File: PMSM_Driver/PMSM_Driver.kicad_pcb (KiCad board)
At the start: 4 copper layers, 261.6 x 144 mm, 276 parts, among them J1 2606-1101, J10 AFBR-2624Z, J11 AFBR-2624Z, J12 AFBR-2624Z, J13 AFBR-2624Z, J14 AFBR-2624Z, J15 AFBR-2624Z, J16 AFBR-2624Z, J17 2606-1101, J18 2606-1101, J2 AFBR-2624Z, J3 1714971, J4 1714971, J5 1827907, J6 AFBR-2624Z, J7 AFBR-2624Z, J8 AFBR-2624Z, J9 AFBR-2624Z, Q1 BC846, Q10 BC846, Q11 RGCL60TK60, Q12 RGCL60TK60, Q13 RGCL60TK60, Q14 RGCL60TK60, Q15 BC846, Q16 RGCL60TK60, Q17 RGCL60TK60, Q18 RGCL60TK60, Q19 RGCL60TK60, Q2 BC846, Q20 BC846, Q21 BC846, Q22 BC846, Q23 BC846, Q24 BC846, Q3 BC846, Q4 BC846, Q5 RGCL60TK60, Q6 RGCL60TK60, Q7 RGCL60TK60, Q8 RGCL60TK60, Q9 BC846, U1 74LVC1G04, U10 HCPL-3120, U11 HCPL-3120, U12 HCPL-3120, U13 74LVC1G04, U14 74LVC1G04, U15 74LVC1G04, U16 MGJ2D051515SC, U17 MGJ2D051515SC, U18 MGJ2D051515SC, U19 HCPL-3120, U2 MGJ2D051515SC, U20 HCPL-3120, U21 HCPL-3120, U22 74LVC1G04, U23 74LVC1G04, U24 74LVC1G04, U25 MGJ2D051515SC, U26 MGJ2D051515SC, U27 MGJ2D051515SC, U28 HCPL-3120, U29 HCPL-3120, U3 HCPL-3120, U30 HCPL-3120, U31 74LVC1G04, U32 74LVC1G04, U33 MGJ2D051515SC, U34 MGJ2D051515SC, U35 HCPL-3120, U36 HCPL-3120, U37 VS-E5TH3006S2L-M3, U38 VS-E5TH3006S2L-M3, U39 VS-E5TH3006S2L-M3, U4 74LVC1G04, U40 VS-E5TH3006S2L-M3, U41 VS-E5TH3006S2L-M3, U42 VS-E5TH3006S2L-M3, U43 VS-E5TH3006S2L-M3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

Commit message: TBC: filled zone to replace 10A traces, phase-A conpleted
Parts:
- moved J17 4.55 mm to (232.4, 159.0)
- moved H2 4.14 mm to (310.4, 44.5)
- moved H4 3.43 mm to (310.9, 176.0)
- moved J18 2.25 mm to (300.3, 158.6)
- moved J1 1.96 mm to (165.4, 159.0)
- moved J5 1.78 mm to (269.4, 50.9)
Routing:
- net GND: track 287.5 -> 142.1 mm, vias 37 -> 36
- net ib_signal: track 0.00 -> 82.8 mm, vias 1 -> 2
- net ic_signal: track 0.00 -> 64.0 mm
- net ia_out: track 110.4 -> 92.2 mm, vias 23 -> 45
- net /A3_E: track 128.5 -> 121.5 mm, vias 2 -> 41
- net ia_signal: track 134.5 -> 139.7 mm, vias 3 -> 2
- net b_out: track 3.88 -> 1.27 mm, vias 1 -> 0
- net GNDREF: vias 123 -> 96
- net /A1_E: vias 12 -> 21
- net -BATT: vias 112 -> 113
- added copper zone on F.Cu, net /A3_E
- added copper zone on In1.Cu, net /A3_E
- added copper zone on In2.Cu, net /A3_E
- added copper zone on In1.Cu, net a_out
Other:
- board size 261.6 x 144 mm -> 265.6 x 144 mm

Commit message: TBC: modify the overlapped filled zone
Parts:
- C1, C2, C3, C4, C5, C6, C9: moved to B.Cu
- moved C9 99.9 mm to (168.4, 51.6)
- moved C6 84.0 mm to (152.5, 51.6)
- moved C5 68.3 mm to (137.1, 51.8)
- moved C4 52.5 mm to (121.4, 51.9)
- moved C3 36.6 mm to (105.6, 52.0)
- moved C2 20.0 mm to (88.8, 52.1)
- moved U39 7.60 mm to (170.9, 79.0)
- moved U41 7.59 mm to (237.9, 78.1)
- moved C1 5.99 mm to (72.5, 52.1)
- moved U37 2.79 mm to (102.6, 84.1)
- moved C20 0.34 mm to (263.3, 93.6)
- moved C26 0.34 mm to (263.3, 91.3)
- moved C32 0.30 mm to (263.2, 89.0)
- moved C33 0.28 mm to (260.4, 89.0)
- moved C27 0.25 mm to (260.4, 91.2)
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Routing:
- net +5V: track 33.8 -> 257.6 mm
- net /B3_E: track 133.1 -> 80.4 mm, vias 2 -> 0
- net /B1_E: track 130.5 -> 84.6 mm, vias 2 -> 26
- net /A1_E: track 128.4 -> 85.1 mm, vias 21 -> 26
- net /A3_E: track 121.5 -> 82.0 mm, vias 41 -> 31
- net /C1_E: track 127.4 -> 92.8 mm, vias 2 -> 18
- net ia_out: track 92.2 -> 66.6 mm, vias 45 -> 23
- net ib_out: track 103.4 -> 78.9 mm, vias 1 -> 8
- net GND: track 142.1 -> 124.6 mm, vias 36 -> 35
- net c_out: track 14.5 -> 0.07 mm, vias 1 -> 0
- net ia_signal: track 139.7 -> 153.2 mm, vias 2 -> 3
- net ic_signal: track 64.0 -> 77.3 mm
- net b_out: track 1.27 -> 0.00 mm
- net ib_signal: track 82.8 -> 84.0 mm
- net ic_out: track 113.9 -> 113.2 mm
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- added copper zone on In2.Cu, net /A1_E
- added copper zone on F.Cu, net /B1_E
- added copper zone on In2.Cu, net /B1_E
- added copper zone on F.Cu, net /C1_E
- added copper zone on In2.Cu, net /C1_E
- added copper zone on F.Cu, net ib_out
- added copper zone on In1.Cu, net ib_out
- removed copper zone on In1.Cu, net /A1_E
- removed copper zone on In2.Cu, net GNDREF
- removed copper zone on In2.Cu, net ia_out
- removed copper zone on F.Cu, net ic_signal

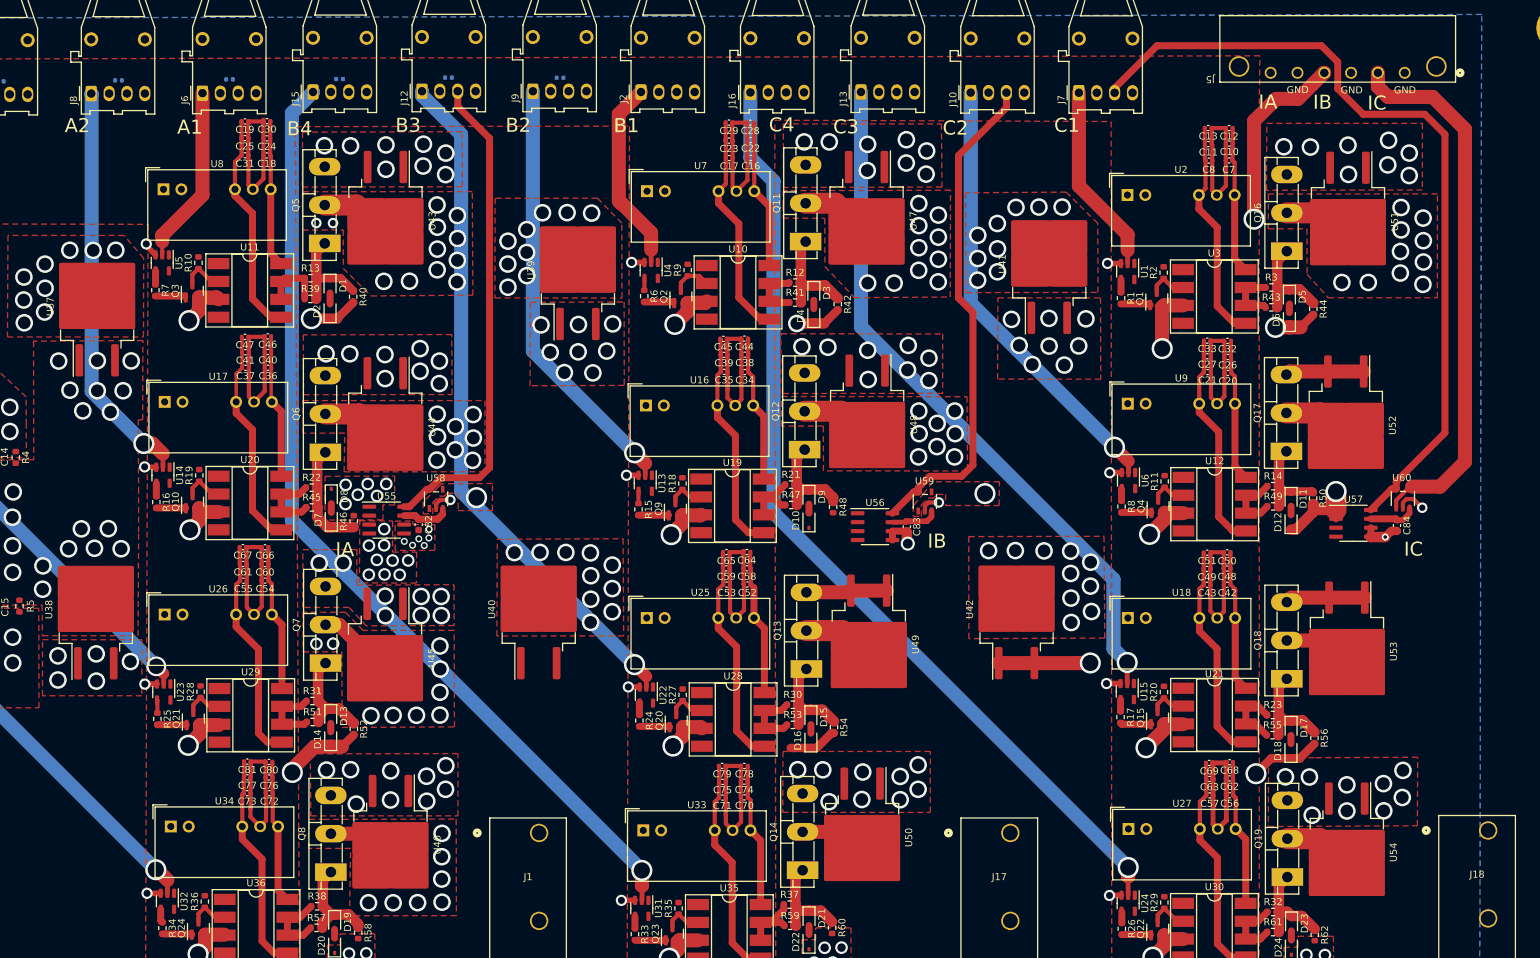
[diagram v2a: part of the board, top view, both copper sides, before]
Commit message: Filled Zone: only Phase C left
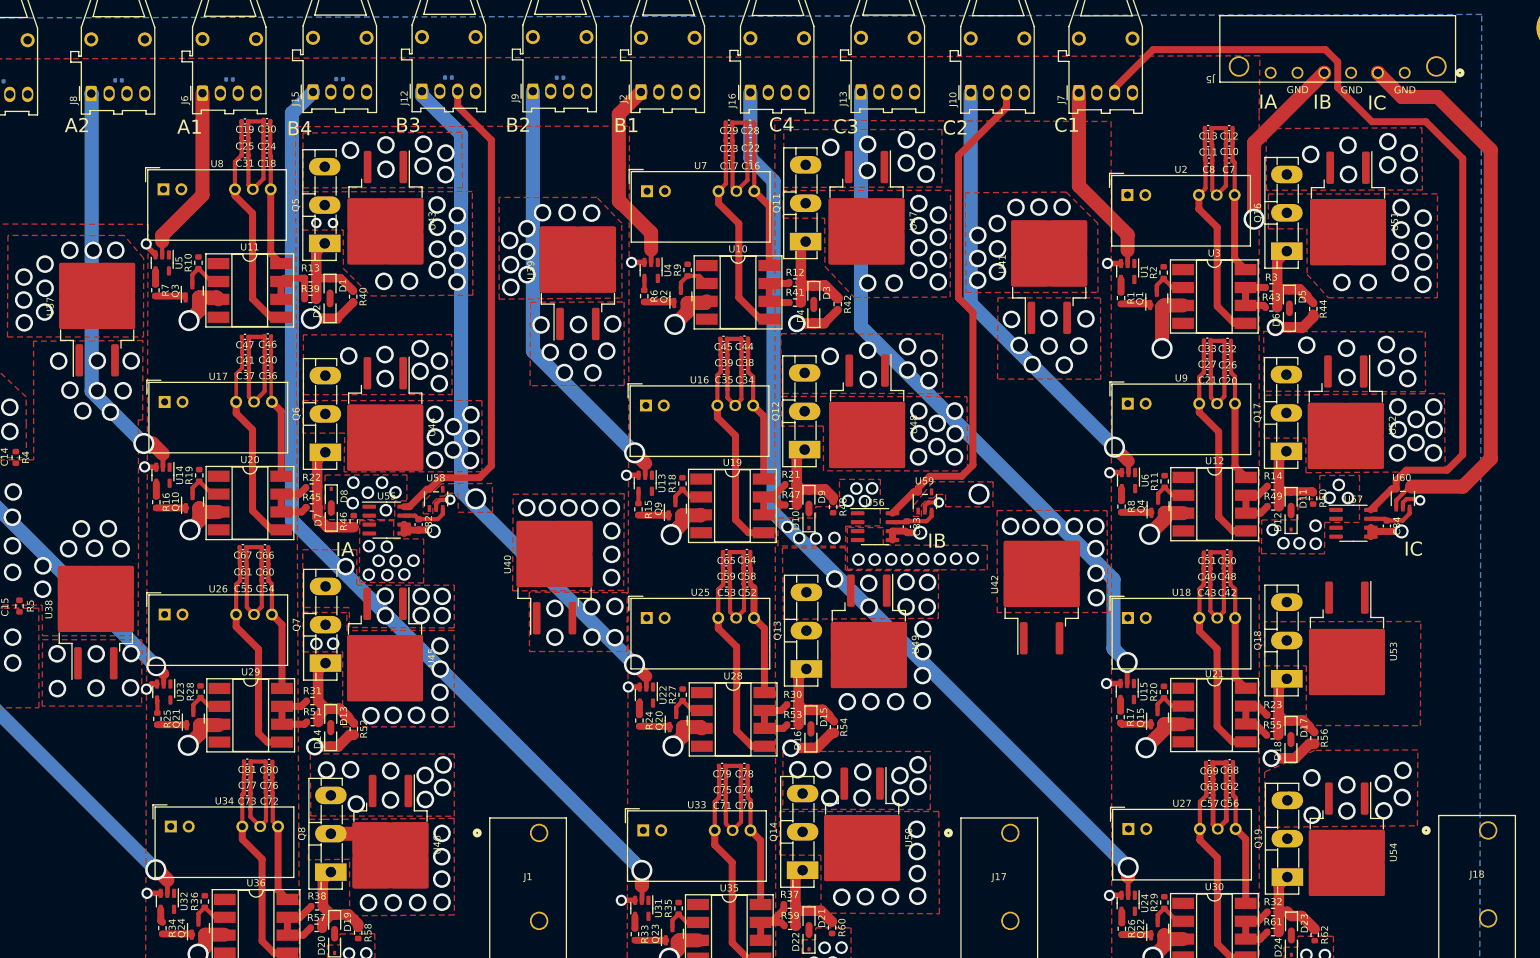
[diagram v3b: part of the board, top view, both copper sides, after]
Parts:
- moved U40 6.77 mm to (167.6, 120.8)
- moved U42 5.02 mm to (236.8, 123.6)
- moved C84 1.43 mm to (285.9, 115.3)
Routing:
- net /C3_E: track 137.7 -> 29.4 mm, vias 2 -> 1
- net ic_out: track 113.2 -> 20.5 mm, vias 1 -> 15
- net /C1_E: track 92.8 -> 28.6 mm, vias 18 -> 25
- net ib_out: track 78.9 -> 23.1 mm, vias 8 -> 22
- net /A1_E: track 85.1 -> 30.3 mm, vias 26 -> 25
- net /B1_E: track 84.6 -> 30.3 mm, vias 26 -> 25
- net /B3_E: track 80.4 -> 28.6 mm, vias 0 -> 31
- net /A3_E: track 82.0 -> 34.4 mm
- net ia_out: track 66.6 -> 23.1 mm, vias 23 -> 22
- net -BATT: track 106.4 -> 66.0 mm, vias 69 -> 68
- net +BATT: track 19.0 -> 0.45 mm
- net ia_signal: track 153.2 -> 162.3 mm, vias 3 -> 2
- net GND: track 124.6 -> 130.3 mm, vias 35 -> 30
- net +5V: track 257.6 -> 262.2 mm
- net ic_signal: track 77.3 -> 81.5 mm
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- added copper zone on F.Cu, net /B3_E
- added copper zone on In1.Cu, net /B3_E
- added copper zone on In2.Cu, net /B3_E
- added copper zone on In1.Cu, net /C3_E
- added copper zone on In2.Cu, net GNDREF
- added copper zone on F.Cu, net b_out
- added copper zone on In1.Cu, net b_out
- added copper zone on F.Cu, net ic_out
- added copper zone on In1.Cu, net ic_out
- removed copper zone on F.Cu, net GND

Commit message: filled zone completed, Fiber-Optic and size of resistors need to be replaced
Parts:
- moved C5 77.8 mm to (61.0, 68.3), turned to -90 degrees
- moved C3 44.9 mm to (63.7, 68.2), turned to -90 degrees
- moved C6 31.3 mm to (121.3, 51.8)
- moved C9 31.2 mm to (137.2, 51.6)
- moved C4 15.8 mm to (105.6, 52.0)
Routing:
- net /C3_E: track 29.4 -> 29.0 mm, vias 1 -> 31
- net ic_out: vias 15 -> 22
- net c_out: vias 0 -> 8
- added copper zone on F.Cu, net /C3_E
- added copper zone on In2.Cu, net /C3_E
- added copper zone on F.Cu, net c_out
- added copper zone on In1.Cu, net c_out

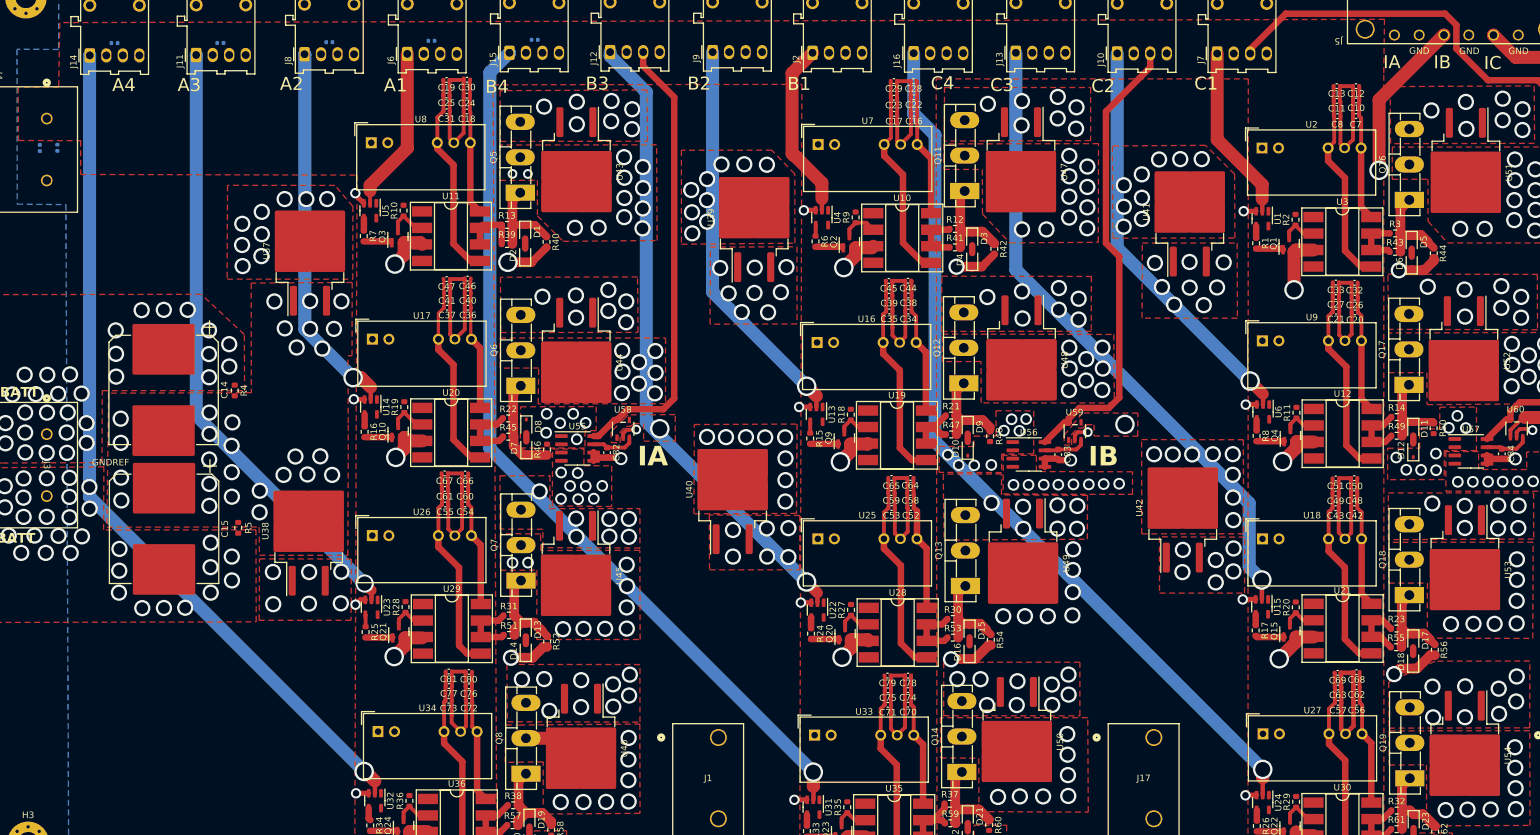
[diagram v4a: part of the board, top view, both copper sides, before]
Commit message: filled zone completed, some SMD components need to be re-selected
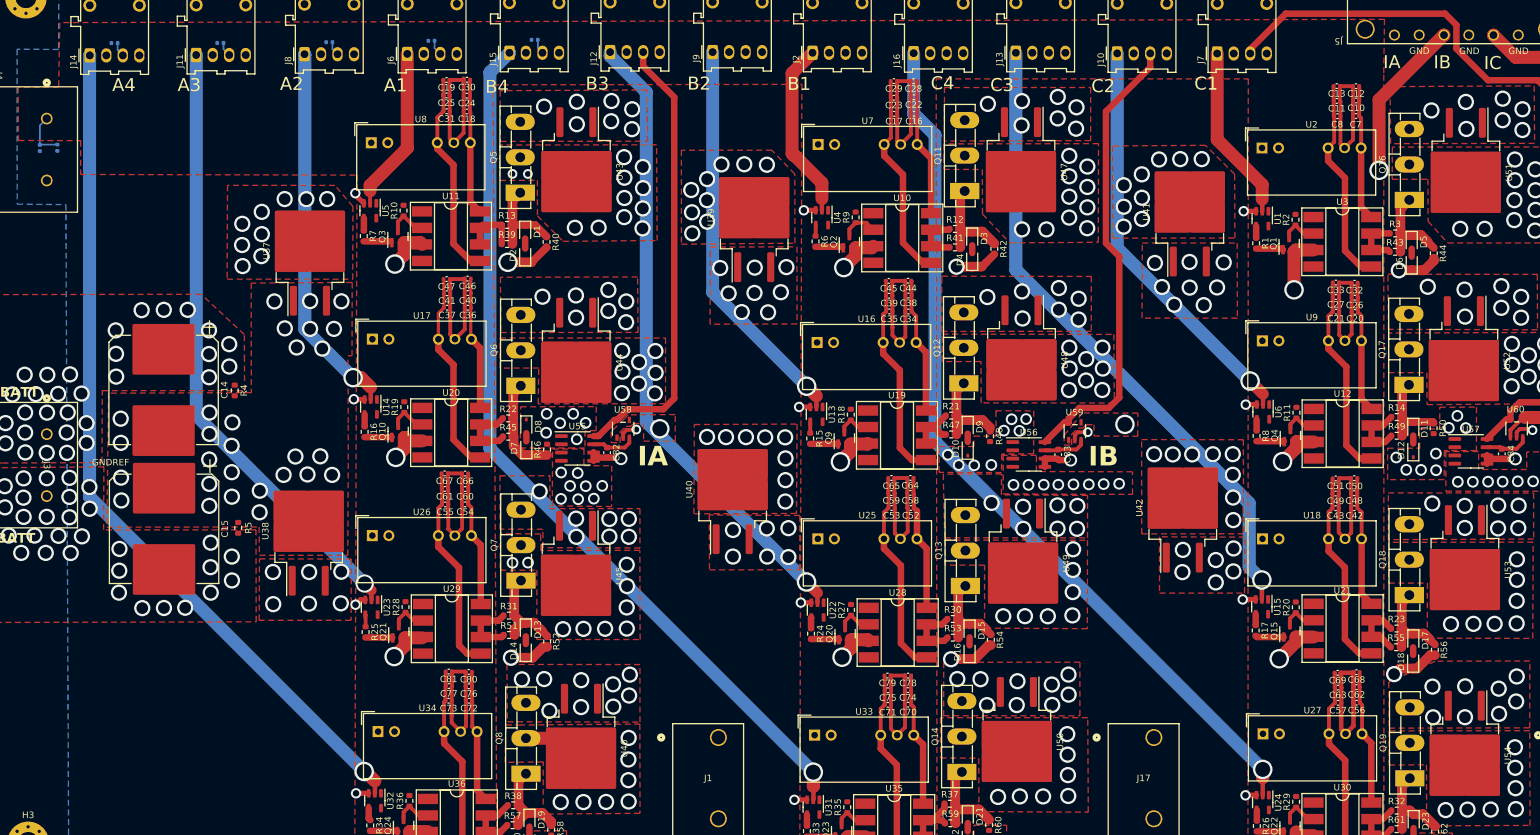
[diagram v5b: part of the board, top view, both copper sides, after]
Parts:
- moved C20 0.08 mm to (263.3, 93.5)
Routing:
- net +5V: track 262.2 -> 280.7 mm
